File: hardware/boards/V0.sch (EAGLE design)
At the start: 137 parts, among them IC2 TPS6300, J1 SJ-43515TS-SMT, J2 HIROSE_DM3BT-DSF-PEJSHIROSE_D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, J3 MOLEX_105450-0101MOLEX_105450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, Q2 ON_SEMI_MMBT5551LT1GON_SEMI_M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, U1 VS1053-L, U2 MICROCHIP_MCP73831T-2ATI-OTMI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, X3 FH12-45S-0.5SH

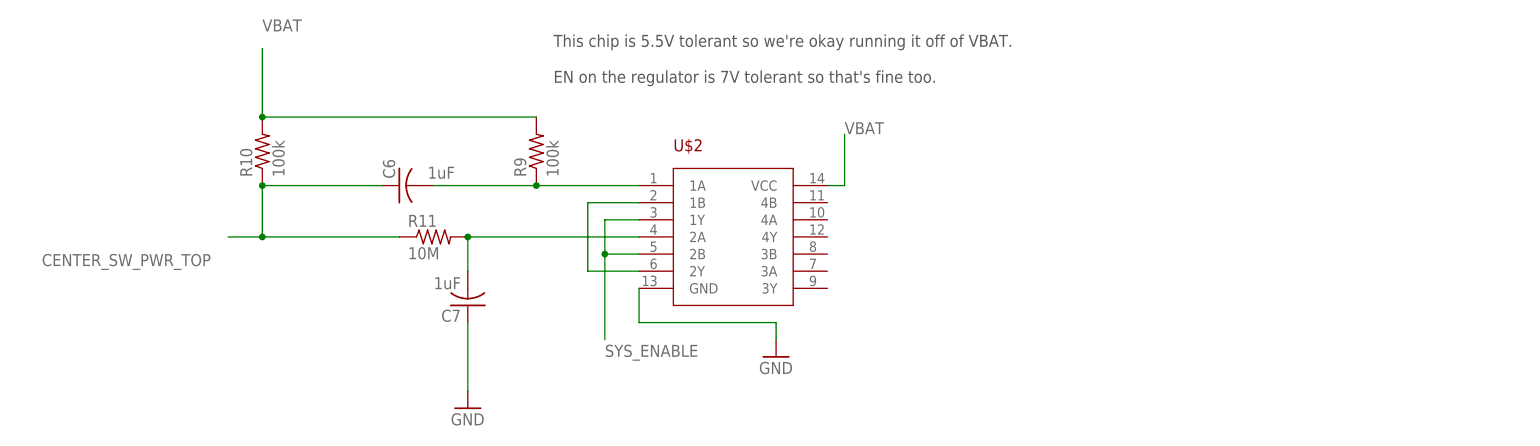
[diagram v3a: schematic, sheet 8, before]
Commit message: Add UVLO protection (using an APX809S-31SA)
Closes #4
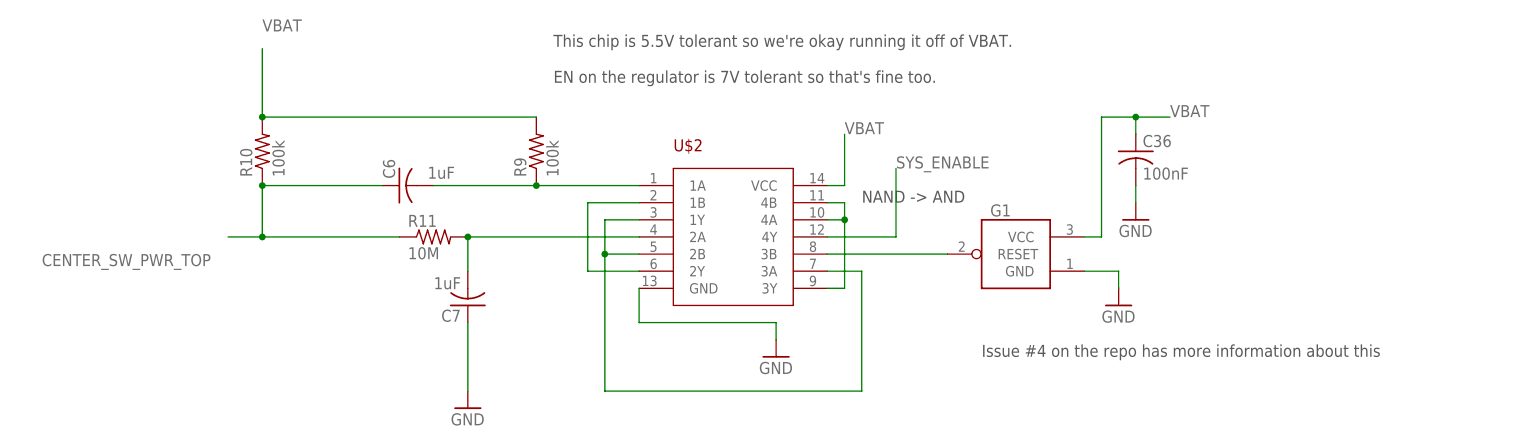
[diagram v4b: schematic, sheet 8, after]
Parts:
- added C36: 100nF, rcl:C-USC1206
- added G1: APX809S-31SA, APX80xx:APX809S-31SA
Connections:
- new net N$12: U$2.1Y, U$2.2B, U$2.3A
- new net N$33: U$2.3Y, U$2.4A, U$2.4B
- new net N$43: G1.RESET, U$2.3B
- net GND: now also C36.2, G1.GND
- net SYS_ENABLE: now also U$2.4Y; no longer U$2.1Y, U$2.2B
- net VBAT: now also C36.1, G1.VCC
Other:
- note added: "Issue #4 on the repo has more information about this"
- note added: "NAND -> AND"
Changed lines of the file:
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@@
 <part name="R52" library="rcl" library_urn="urn:adsk.eagle:library:334" deviceset="R-US_" device="R0805" package3d_urn="urn:adsk.eagle:package:23553/2" value="360k"/>
 <part name="GND46" library="supply1" library_urn="urn:adsk.eagle:library:371" deviceset="GND" device=""/>
+<part name="G1" library="APX80xx" deviceset="APX809S" device="-31SA" package3d_urn="urn:adsk.eagle:package:28738/2"/>
+<part name="GND47" library="supply1" library_urn="urn:adsk.eagle:library:371" deviceset="GND" device=""/>
+<part name="C36" library="rcl" library_urn="urn:adsk.eagle:library:334" deviceset="C-US" device="C1206" package3d_urn="urn:adsk.eagle:package:23618/2" value="100nF"/>
+<part name="GND48" library="supply1" library_urn="urn:adsk.eagle:library:371" deviceset="GND" device=""/>
 </parts>
 <sheets>
@@
 <text x="0" y="38.1" size="1.778" layer="97">This chip is 5.5V tolerant so we're okay running it off of VBAT.
 EN on the regulator is 7V tolerant so that's fine too.</text>
+<text x="63.5" y="-2.54" size="1.778" layer="97">Issue #4 on the repo has more information about this</text>
+<text x="45.72" y="20.32" size="1.778" layer="97">NAND -&gt; AND</text>
 </plain>
 <instances>
@@
 <instance part="GND33" gate="1" x="33.02" y="-2.54" smashed="yes">
 <attribute name="VALUE" x="30.48" y="-5.08" size="1.778" layer="96"/>
+</instance>
+<instance part="G1" gate="G$1" x="68.58" y="12.7" smashed="yes" rot="MR0">
+<attribute name="NAME" x="64.77" y="20.066" size="1.778" layer="95" rot="MR180"/>
+</instance>
+<instance part="GND47" gate="1" x="83.82" y="5.08" smashed="yes">
+<attribute name="VALUE" x="81.28" y="2.54" size="1.778" layer="96"/>
+</instance>
+<instance part="C36" gate="G$1" x="86.36" y="27.94" smashed="yes">
+<attribute name="NAME" x="87.376" y="28.575" size="1.778" layer="95"/>
+<attribute name="VALUE" x="87.376" y="23.749" size="1.778" layer="96"/>
+</instance>
+<instance part="GND48" gate="1" x="86.36" y="17.78" smashed="yes">
+<attribute name="VALUE" x="83.82" y="15.24" size="1.778" layer="96"/>
 </instance>
 </instances>
@@
 </segment>
 </net>
-<net name="SYS_ENABLE" class="0">
-<segment>
-<pinref part="U$2" gate="G$1" pin="1Y"/>
-<wire x1="12.7" y1="17.78" x2="7.62" y2="17.78" width="0.1524" layer="91"/>
-<wire x1="7.62" y1="17.78" x2="7.62" y2="12.7" width="0.1524" layer="91"/>
-<pinref part="U$2" gate="G$1" pin="2B"/>
-<wire x1="7.62" y1="12.7" x2="12.7" y2="12.7" width="0.1524" layer="91"/>
-<wire x1="7.62" y1="12.7" x2="7.62" y2="0" width="0.1524" layer="91"/>
-<junction x="7.62" y="12.7"/>
-<label x="7.62" y="-2.54" size="1.778" layer="95"/>
-</segment>
-</net>
 <net name="N$19" class="0">
 <segment>
@@
 <junction x="-43.18" y="33.02"/>
 <label x="-43.18" y="45.72" size="1.778" layer="95"/>
+</segment>
+<segment>
+<pinref part="G1" gate="G$1" pin="VCC"/>
+<wire x1="78.74" y1="15.24" x2="81.28" y2="15.24" width="0.1524" layer="91"/>
+<wire x1="81.28" y1="15.24" x2="81.28" y2="33.02" width="0.1524" layer="91"/>
+<wire x1="81.28" y1="33.02" x2="86.36" y2="33.02" width="0.1524" layer="91"/>
+<label x="91.44" y="33.02" size="1.778" layer="95"/>
+<pinref part="C36" gate="G$1" pin="1"/>
+<wire x1="86.36" y1="33.02" x2="91.44" y2="33.02" width="0.1524" layer="91"/>
+<wire x1="86.36" y1="30.48" x2="86.36" y2="33.02" width="0.1524" layer="91"/>
+<junction x="86.36" y="33.02"/>
 </segment>
 </net>
@@
 <pinref part="GND33" gate="1" pin="GND"/>
 </segment>
-</net>
+<segment>
+<pinref part="G1" gate="G$1" pin="GND"/>
+<wire x1="78.74" y1="10.16" x2="83.82" y2="10.16" width="0.1524" layer="91"/>
+<pinref part="GND47" gate="1" pin="GND"/>
+<wire x1="83.82" y1="10.16" x2="83.82" y2="7.62" width="0.1524" layer="91"/>
+</segment>
+<segment>
+<pinref part="GND48" gate="1" pin="GND"/>
+<pinref part="C36" gate="G$1" pin="2"/>
+<wire x1="86.36" y1="20.32" x2="86.36" y2="22.86" width="0.1524" layer="91"/>
+</segment>
+</net>
+<net name="N$12" class="0">
+<segment>
+<pinref part="U$2" gate="G$1" pin="1Y"/>
+<wire x1="12.7" y1="17.78" x2="7.62" y2="17.78" width="0.1524" layer="91"/>
+<wire x1="7.62" y1="17.78" x2="7.62" y2="12.7" width="0.1524" layer="91"/>
+<pinref part="U$2" gate="G$1" pin="2B"/>
+<wire x1="7.62" y1="12.7" x2="12.7" y2="12.7" width="0.1524" layer="91"/>
+<wire x1="7.62" y1="12.7" x2="7.62" y2="-7.62" width="0.1524" layer="91"/>
+<junction x="7.62" y="12.7"/>
+<wire x1="7.62" y1="-7.62" x2="45.72" y2="-7.62" width="0.1524" layer="91"/>
+<pinref part="U$2" gate="G$1" pin="3A"/>
+<wire x1="45.72" y1="-7.62" x2="45.72" y2="10.16" width="0.1524" layer="91"/>
+<wire x1="45.72" y1="10.16" x2="40.64" y2="10.16" width="0.1524" layer="91"/>
+</segment>
+</net>
+<net name="N$33" class="0">
+<segment>
+<pinref part="U$2" gate="G$1" pin="3Y"/>
+<wire x1="40.64" y1="7.62" x2="43.18" y2="7.62" width="0.1524" layer="91"/>
+<wire x1="43.18" y1="7.62" x2="43.18" y2="17.78" width="0.1524" layer="91"/>
+<pinref part="U$2" gate="G$1" pin="4B"/>
+<wire x1="43.18" y1="17.78" x2="43.18" y2="20.32" width="0.1524" layer="91"/>
+<wire x1="43.18" y1="20.32" x2="40.64" y2="20.32" width="0.1524" layer="91"/>
+<pinref part="U$2" gate="G$1" pin="4A"/>
+<wire x1="43.18" y1="17.78" x2="40.64" y2="17.78" width="0.1524" layer="91"/>
+<junction x="43.18" y="17.78"/>
+</segment>
+</net>
+<net name="SYS_ENABLE" class="0">
+<segment>
+<pinref part="U$2" gate="G$1" pin="4Y"/>
+<wire x1="40.64" y1="15.24" x2="50.8" y2="15.24" width="0.1524" layer="91"/>
+<wire x1="50.8" y1="15.24" x2="50.8" y2="25.4" width="0.1524" layer="91"/>
+<label x="50.8" y="25.4" size="1.778" layer="95"/>
+</segment>
+</net>
+<net name="N$43" class="0">
+<segment>
+<pinref part="G1" gate="G$1" pin="RESET"/>
+<pinref part="U$2" gate="G$1" pin="3B"/>
+<wire x1="58.42" y1="12.7" x2="40.64" y2="12.7" width="0.1524" layer="91"/>
+</segment>
+</net>

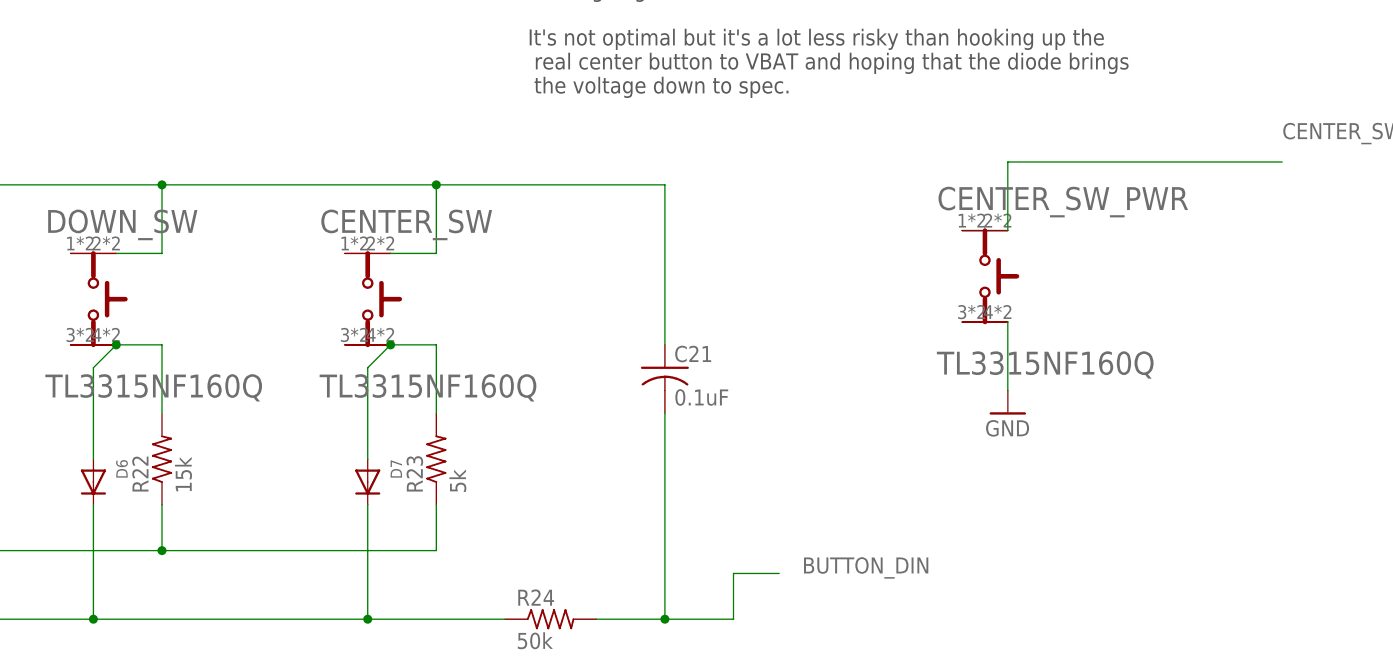
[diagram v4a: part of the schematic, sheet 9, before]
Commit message: Swap center buttons for 100Q (lower actuation force) variants
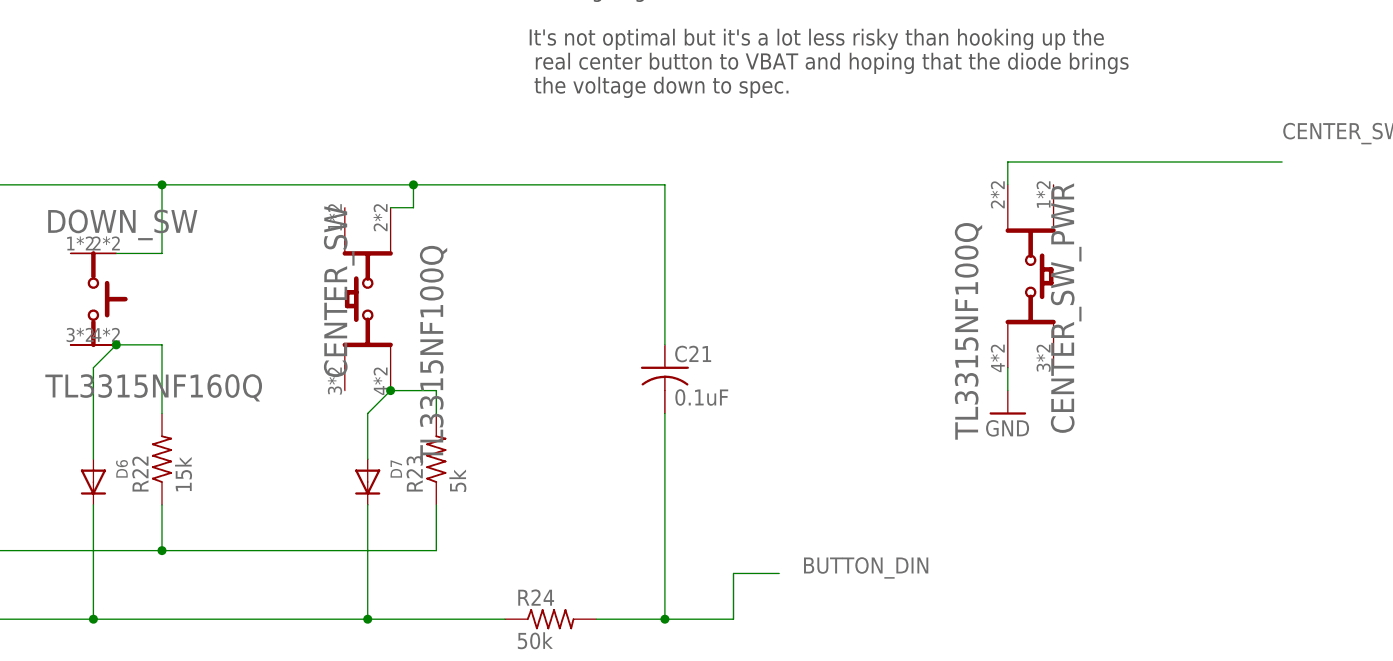
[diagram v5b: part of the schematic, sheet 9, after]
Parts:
- CENTER_SW, CENTER_SW_PWR: value E-SWITCH_TL3315NF160QE-SWITCH_TL3315NF160Q_0_0 -> E-SWITCH_TL3315NF100QE-SWITCH_TL3315NF100Q_0_0; device E-Switch-TL3315NF160Q:E-SWITCH_TL3315NF160QE-SWITCH_TL3315NF160Q_0_0 -> E-Switch-TL3315NF100Q:E-SWITCH_TL3315NF100QE-SWITCH_TL3315NF100Q_0_0
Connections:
- net CENTER_SW renamed N$44
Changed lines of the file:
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@@
 </part>
 <part name="DOWN_SW" library="E-Switch-TL3315NF160Q" deviceset="E-SWITCH_TL3315NF160Q" device="E-SWITCH_TL3315NF160Q_0_0"/>
-<part name="CENTER_SW" library="E-Switch-TL3315NF160Q" deviceset="E-SWITCH_TL3315NF160Q" device="E-SWITCH_TL3315NF160Q_0_0"/>
+<part name="CENTER_SW" library="E-Switch-TL3315NF100Q" deviceset="E-SWITCH_TL3315NF100Q" device="E-SWITCH_TL3315NF100Q_0_0"/>
 <part name="LEFT_SW" library="E-Switch-TL3315NF160Q" deviceset="E-SWITCH_TL3315NF160Q" device="E-SWITCH_TL3315NF160Q_0_0">
 <attribute name="SPICEPREFIX" value="E"/>
@@
 <part name="R35" library="rcl" library_urn="urn:adsk.eagle:library:334" deviceset="R-US_" device="R0805" package3d_urn="urn:adsk.eagle:package:23553/2" value="100"/>
 <part name="R36" library="rcl" library_urn="urn:adsk.eagle:library:334" deviceset="R-US_" device="R0805" package3d_urn="urn:adsk.eagle:package:23553/2" value="50"/>
-<part name="CENTER_SW_PWR" library="E-Switch-TL3315NF160Q" deviceset="E-SWITCH_TL3315NF160Q" device="E-SWITCH_TL3315NF160Q_0_0"/>
+<part name="CENTER_SW_PWR" library="E-Switch-TL3315NF100Q" deviceset="E-SWITCH_TL3315NF100Q" device="E-SWITCH_TL3315NF100Q_0_0"/>
 <part name="GND31" library="supply1" library_urn="urn:adsk.eagle:library:371" deviceset="GND" device=""/>
 <part name="GND32" library="supply1" library_urn="urn:adsk.eagle:library:371" deviceset="GND" device=""/>
@@
 <attribute name="NAME" x="32.766" y="30.226" size="2.54" layer="95" align="top-left"/>
 </instance>
-<instance part="CENTER_SW" gate="G$0" x="66.04" y="30.48" smashed="yes">
-<attribute name="NAME" x="63.246" y="30.226" size="2.54" layer="95" align="top-left"/>
+<instance part="CENTER_SW" gate="G$0" x="63.5" y="27.94" smashed="yes" rot="MR270">
+<attribute name="NAME" x="63.754" y="30.734" size="2.54" layer="95" rot="MR270" align="top-left"/>
 </instance>
 <instance part="LEFT_SW" gate="G$0" x="-63.5" y="30.48" smashed="yes">
@@
 <attribute name="VALUE" x="64.77" y="2.54" size="1.27" layer="96" rot="R270"/>
 </instance>
-<instance part="CENTER_SW_PWR" gate="G$0" x="134.62" y="33.02" smashed="yes">
-<attribute name="NAME" x="131.826" y="32.766" size="2.54" layer="95" align="top-left"/>
+<instance part="CENTER_SW_PWR" gate="G$0" x="147.32" y="30.48" smashed="yes" rot="R270">
+<attribute name="NAME" x="147.066" y="33.274" size="2.54" layer="95" rot="R270" align="top-left"/>
 </instance>
 <instance part="GND31" gate="1" x="139.7" y="7.62" smashed="yes">
@@
 <wire x1="0" y1="33.02" x2="12.7" y2="33.02" width="0.1524" layer="91"/>
 <wire x1="12.7" y1="33.02" x2="45.72" y2="33.02" width="0.1524" layer="91"/>
-<wire x1="45.72" y1="33.02" x2="76.2" y2="33.02" width="0.1524" layer="91"/>
+<wire x1="45.72" y1="33.02" x2="73.66" y2="33.02" width="0.1524" layer="91"/>
+<wire x1="73.66" y1="33.02" x2="101.6" y2="33.02" width="0.1524" layer="91"/>
 <wire x1="-25.4" y1="25.4" x2="-20.32" y2="25.4" width="0.1524" layer="91"/>
 <wire x1="-20.32" y1="25.4" x2="-20.32" y2="33.02" width="0.1524" layer="91"/>
@@
 <wire x1="45.72" y1="25.4" x2="45.72" y2="33.02" width="0.1524" layer="91"/>
 <junction x="45.72" y="33.02"/>
-<pinref part="CENTER_SW" gate="G$0" pin="2"/>
-<wire x1="71.12" y1="25.4" x2="76.2" y2="25.4" width="0.1524" layer="91"/>
-<wire x1="76.2" y1="25.4" x2="76.2" y2="33.02" width="0.1524" layer="91"/>
 <wire x1="0" y1="33.02" x2="0" y2="40.64" width="0.1524" layer="91"/>
 <wire x1="0" y1="40.64" x2="7.62" y2="40.64" width="0.1524" layer="91"/>
 <junction x="0" y="33.02"/>
 <label x="10.16" y="40.64" size="1.778" layer="95"/>
-<wire x1="76.2" y1="33.02" x2="101.6" y2="33.02" width="0.1524" layer="91"/>
-<junction x="76.2" y="33.02"/>
 <pinref part="C21" gate="G$1" pin="1"/>
 <wire x1="101.6" y1="33.02" x2="101.6" y2="15.24" width="0.1524" layer="91"/>
+<pinref part="CENTER_SW" gate="G$0" pin="2"/>
+<wire x1="71.12" y1="30.48" x2="73.66" y2="30.48" width="0.1524" layer="91"/>
+<wire x1="73.66" y1="30.48" x2="73.66" y2="33.02" width="0.1524" layer="91"/>
+<junction x="73.66" y="33.02"/>
 </segment>
 </net>
@@
 <pinref part="CENTER_SW_PWR" gate="G$0" pin="4"/>
 <pinref part="GND31" gate="1" pin="GND"/>
-<wire x1="139.7" y1="17.78" x2="139.7" y2="10.16" width="0.1524" layer="91"/>
+<wire x1="139.7" y1="12.7" x2="139.7" y2="10.16" width="0.1524" layer="91"/>
 </segment>
 </net>
@@
 </segment>
 </net>
-<net name="CENTER_SW" class="0">
-<segment>
-<pinref part="R23" gate="G$1" pin="2"/>
-<pinref part="CENTER_SW" gate="G$0" pin="4"/>
-<wire x1="71.12" y1="15.24" x2="76.2" y2="15.24" width="0.1524" layer="91"/>
-<wire x1="76.2" y1="15.24" x2="76.2" y2="7.62" width="0.1524" layer="91"/>
-<pinref part="D7" gate="G$1" pin="A"/>
-<wire x1="68.58" y1="2.54" x2="68.58" y2="12.7" width="0.1524" layer="91"/>
-<wire x1="68.58" y1="12.7" x2="71.12" y2="15.24" width="0.1524" layer="91"/>
-<junction x="71.12" y="15.24"/>
-</segment>
-</net>
 <net name="CENTER_SW_PWR_TOP" class="0">
 <segment>
 <pinref part="CENTER_SW_PWR" gate="G$0" pin="2"/>
-<wire x1="139.7" y1="27.94" x2="139.7" y2="35.56" width="0.1524" layer="91"/>
+<wire x1="139.7" y1="33.02" x2="139.7" y2="35.56" width="0.1524" layer="91"/>
 <wire x1="139.7" y1="35.56" x2="170.18" y2="35.56" width="0.1524" layer="91"/>
 <label x="170.18" y="38.1" size="1.778" layer="95"/>
 </segment>
 </net>
+<net name="N$44" class="0">
+<segment>
+<pinref part="D7" gate="G$1" pin="A"/>
+<wire x1="68.58" y1="2.54" x2="68.58" y2="7.62" width="0.1524" layer="91"/>
+<pinref part="CENTER_SW" gate="G$0" pin="4"/>
+<wire x1="68.58" y1="7.62" x2="71.12" y2="10.16" width="0.1524" layer="91"/>
+<pinref part="R23" gate="G$1" pin="2"/>
+<wire x1="76.2" y1="7.62" x2="76.2" y2="10.16" width="0.1524" layer="91"/>
+<wire x1="76.2" y1="10.16" x2="71.12" y2="10.16" width="0.1524" layer="91"/>
+<junction x="71.12" y="10.16"/>
+</segment>
+</net>

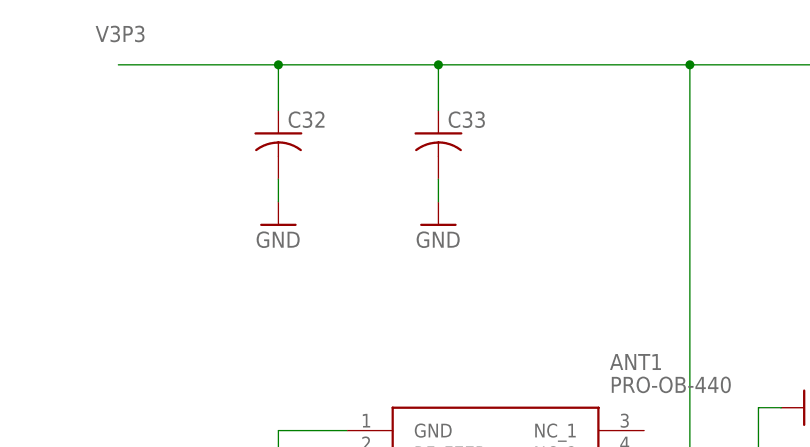
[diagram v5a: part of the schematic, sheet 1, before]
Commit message: add missing esp32 capacitor values
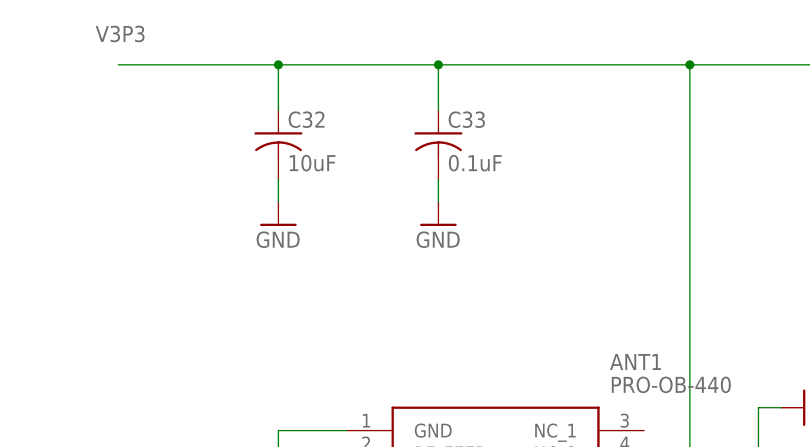
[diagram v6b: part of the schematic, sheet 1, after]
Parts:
- C32: value (none) -> 10uF
- C33: value (none) -> 0.1uF
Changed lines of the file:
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@@
 <part name="R48" library="rcl" library_urn="urn:adsk.eagle:library:334" deviceset="R-US_" device="R0805" package3d_urn="urn:adsk.eagle:package:23553/2" value="10k"/>
 <part name="R49" library="rcl" library_urn="urn:adsk.eagle:library:334" deviceset="R-US_" device="R0805" package3d_urn="urn:adsk.eagle:package:23553/2" value="10k"/>
-<part name="C32" library="rcl" library_urn="urn:adsk.eagle:library:334" deviceset="C-US" device="C1206" package3d_urn="urn:adsk.eagle:package:23618/2"/>
-<part name="C33" library="rcl" library_urn="urn:adsk.eagle:library:334" deviceset="C-US" device="C1206" package3d_urn="urn:adsk.eagle:package:23618/2"/>
+<part name="C32" library="rcl" library_urn="urn:adsk.eagle:library:334" deviceset="C-US" device="C1206" package3d_urn="urn:adsk.eagle:package:23618/2" value="10uF"/>
+<part name="C33" library="rcl" library_urn="urn:adsk.eagle:library:334" deviceset="C-US" device="C1206" package3d_urn="urn:adsk.eagle:package:23618/2" value="0.1uF"/>
 <part name="GND41" library="supply1" library_urn="urn:adsk.eagle:library:371" deviceset="GND" device=""/>
 <part name="GND42" library="supply1" library_urn="urn:adsk.eagle:library:371" deviceset="GND" device=""/>
